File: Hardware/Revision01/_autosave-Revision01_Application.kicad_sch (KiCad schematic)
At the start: 76 parts, among them J2 StrainConn, J3 StrainConn, J4 StrainConn, J5 StrainConn, J6 StrainConn, J7 StrainConn, J8 StrainConn, J9 StrainConn, Q1 PMOS, Q2 NMOS, Q3 PMOS, U2 MRF89XAM9AT-I/RM, U3 ICM-45605

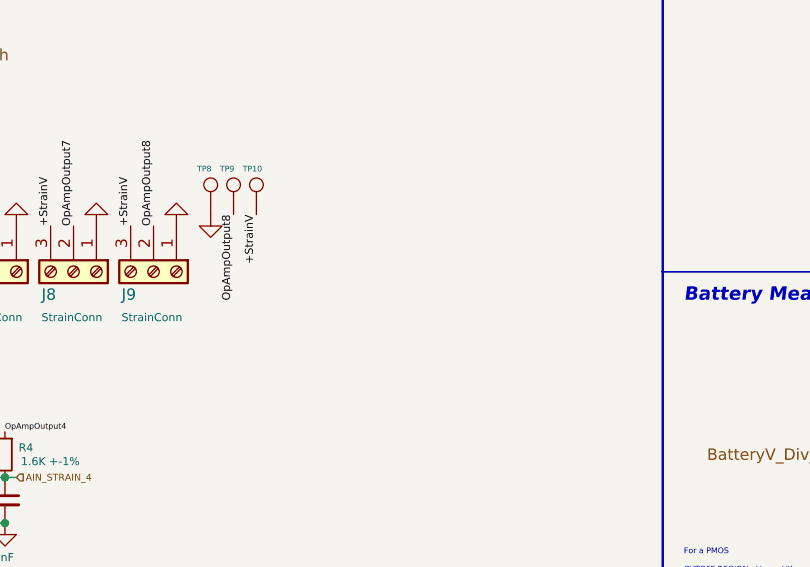
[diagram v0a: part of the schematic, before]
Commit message: rewired and re-routed traces on strainAmplifier
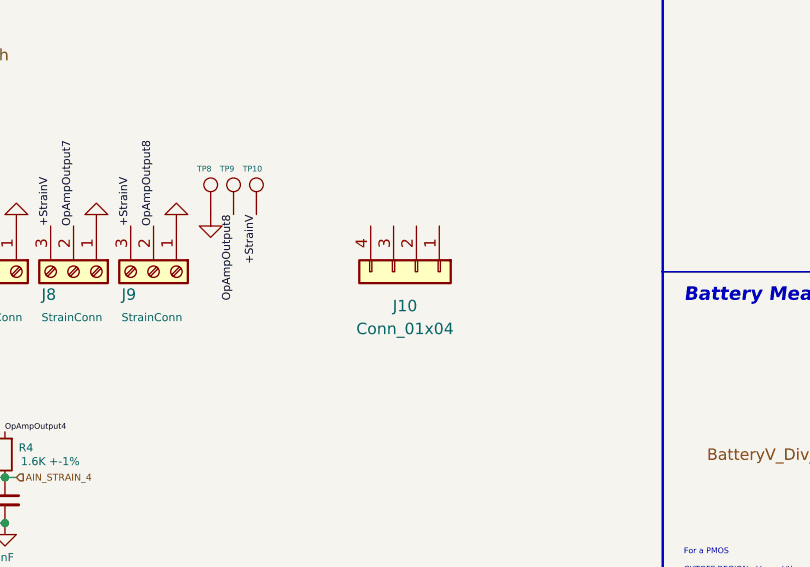
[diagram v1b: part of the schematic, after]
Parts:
- added J10: Conn_01x04, symbol Connector_Generic:Conn_01x04
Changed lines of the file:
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@@
 			"RABnADgAdwA0AG0AcwBHAG8AMgBvAG4AeQBRAEQAegBKAEQAcgBtAGcASwBxAFgAWgBaAG4AMQBn"
 			"ADEAWABDAFEARgBVAEYASQB1AFYALwBFAEEARgBPAFoAZwBsAGEAbQBuAGwAdABJAFQARABBAFMA"
-			"LwB1ADcAMQA2AC8Adg=="
+			"LwB1ADcAMQA2AC8AdgBRAE4AVgBjAFEAdABYAGsAcwBxAHIATABxAG8AQwBxAGgAWQBYAE8AcwAx"
+			"ADgAbgBlADEAQQBWAG0AZABxAHkALwBoAGUAVABOAEsAcQBMAEIAbwBRAGoAMwA4AEYARQBNADgA"
+			"TgBsADYAaABXAFgAUQBkAG0ANABkADUAeABuAC8ASABnAG0AQQBXADMAdgBvAEIAWQBKADMAZwBG"
+			"AHQAUgBCAG8ARgBSADUASQB3AHUAcwBKADMAOQB6AGcAcgA5AC8AZwBQAC8ANABOACsAYQA5AEkA"
+			"aQBmAHUAYgB5AFYASwBhAGQAagBNAEkAKwBKAEYARABSAFIAOAAwAFoAMgB5AHkATwB1AGkAUwBC"
+			"AFAAcQB6ADIATgBqACsAZQBhADQAegB1AE0AcQBpAHgANAB5AGUAWQBjAFQAUQA4AGIAUABWADUA"
+			"TgBCAFUAOQBzADYAagBSAFEAaQAzAFkAeQByAFcASABYAG8AWgBBAHAAZABiAHcAdQBlAHoAVgBt"
+			"ADkAcgByAFcAMwBBAHQASQBOAEsAQgBnADgANwBJADkAOQBiAHEAUwB3AEgAUABqAHYAMABjAFcA"
+			"dABVADIAZABsAHgARQB6AGEAMgBpADIARgBJAFQANABzAHEANQAzAEEAMQBuAHAAVABDAEsAdgBx"
+			"ADcAZgBkAFcARQByAE8AMABSAEcARQBlAE0ASABkADIAdwAvAHoATABsAHAAOAAxAHkAdQBYAE8A"
+			"bgB5ADIAdQA5ADcAWgBYADkAVgBxACsAWABpAC8AUgB3ADEAZAA2AEgAbgBtAFYANABkAHMAUwBZ"
+			"AFYAZwBPAGIAVgAxADYAeQBuAEsATQA4AHEAQgBkAEgAeABZAGUAOQBTAHkAawBYAEgASQB2AG0A"
+			"cABIAFoAcwB0AHQAbABtAG0AMgAyADIAMgBXAFoAZgBoAEcAMgBrAGMAcgBQAE4AZgBnAGYAVwBQ"
+			"AGEATgBnAFIAKwBFAE8AYQBJAEUAYgBNAEMAZwByAE0AWABoAHIAOABkADAAdgA3ADMAdABYADcA"
+			"MgBpADAANwBzAEcAeAByAEEAcQBrAHQAZABNAFMASwByADgAUQBCAHgAVwBCADAATABpAEMAQgBG"
+			"AG4AYwBsADQAbwBwAE8AVQBBAGsAUQBSAGwAdwB3ADcAdwAzAHYAYgBuAFIAbgA5AC8AaQBlAE0A"
+			"UwBVADgATgBVAHIALwBQAFEASgBIAHcANgBZADUAMABaAEMAWQB4ADcAOQBGAGEAQQBoAEEARgBn"
+			"AHMAQwBXAEUATwBPAHMAegBEAGEAVwBkAFYAYgB5AEgAVgA2AGYAMgBsAHEAcQBrAGMAUgBXAFIA"
+			"cgBSAG4ARABOAFAARg=="
 		)
 	)
@@
 					(unit 1)
 				)
+			)
+		)
+	)
+	(symbol
+		(lib_id "Connector_Generic:Conn_01x04")
+		(at 149.86 114.3 270)
+		(unit 1)
+		(exclude_from_sim no)
+		(in_bom yes)
+		(on_board yes)
+		(dnp no)
+		(fields_autoplaced yes)
+		(property "Reference" "J10"
+			(at 148.59 118.11 90)
+			(effects
+				(font
+					(size 1.27 1.27)
+				)
+			)
+		)
+		(property "Value" "Conn_01x04"
+			(at 148.59 120.65 90)
+			(effects
+				(font
+					(size 1.27 1.27)
+				)
+			)
+		)
+		(property "Footprint" ""
+			(at 149.86 114.3 0)
+			(effects
+				(font
+					(size 1.27 1.27)
+				)
+				(hide yes)
+			)
+		)
+		(property "Datasheet" "~"
+			(at 149.86 114.3 0)
+			(effects
+				(font
+					(size 1.27 1.27)
+				)
+				(hide yes)
+			)
+		)
+		(property "Description" "Generic connector, single row, 01x04, script generated (kicad-library-utils/schlib/autogen/connector/)"
+			(at 149.86 114.3 0)
+			(effects
+				(font
+					(size 1.27 1.27)
+				)
+				(hide yes)
+			)
+		)
+		(pin "2"
+		)
+		(pin "4"
+		)
+		(pin "1"
+		)
+		(pin "3"
+		)
+		(instances
+			(project "Revision01"
+				(path "/955cc99e-a129-42cf-abc7-aa99813fdb5f/00000000-0000-0000-0000-00005eb1de63"
+					(reference "J10")
+					(unit 1)
+				)
